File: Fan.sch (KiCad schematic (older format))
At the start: 0 parts

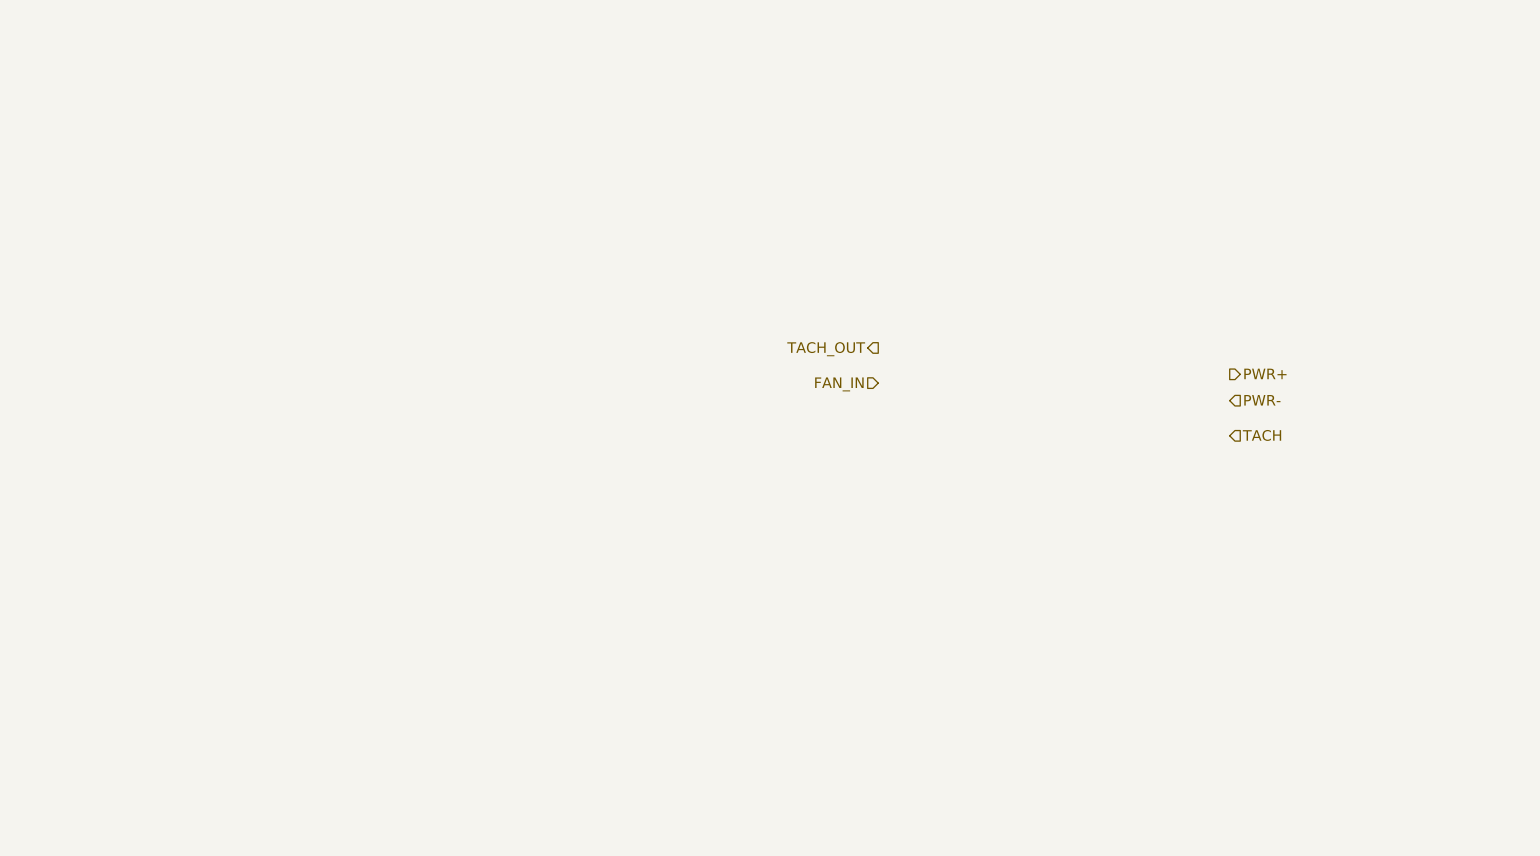
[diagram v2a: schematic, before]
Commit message: Created first schematic for Fan Driver module
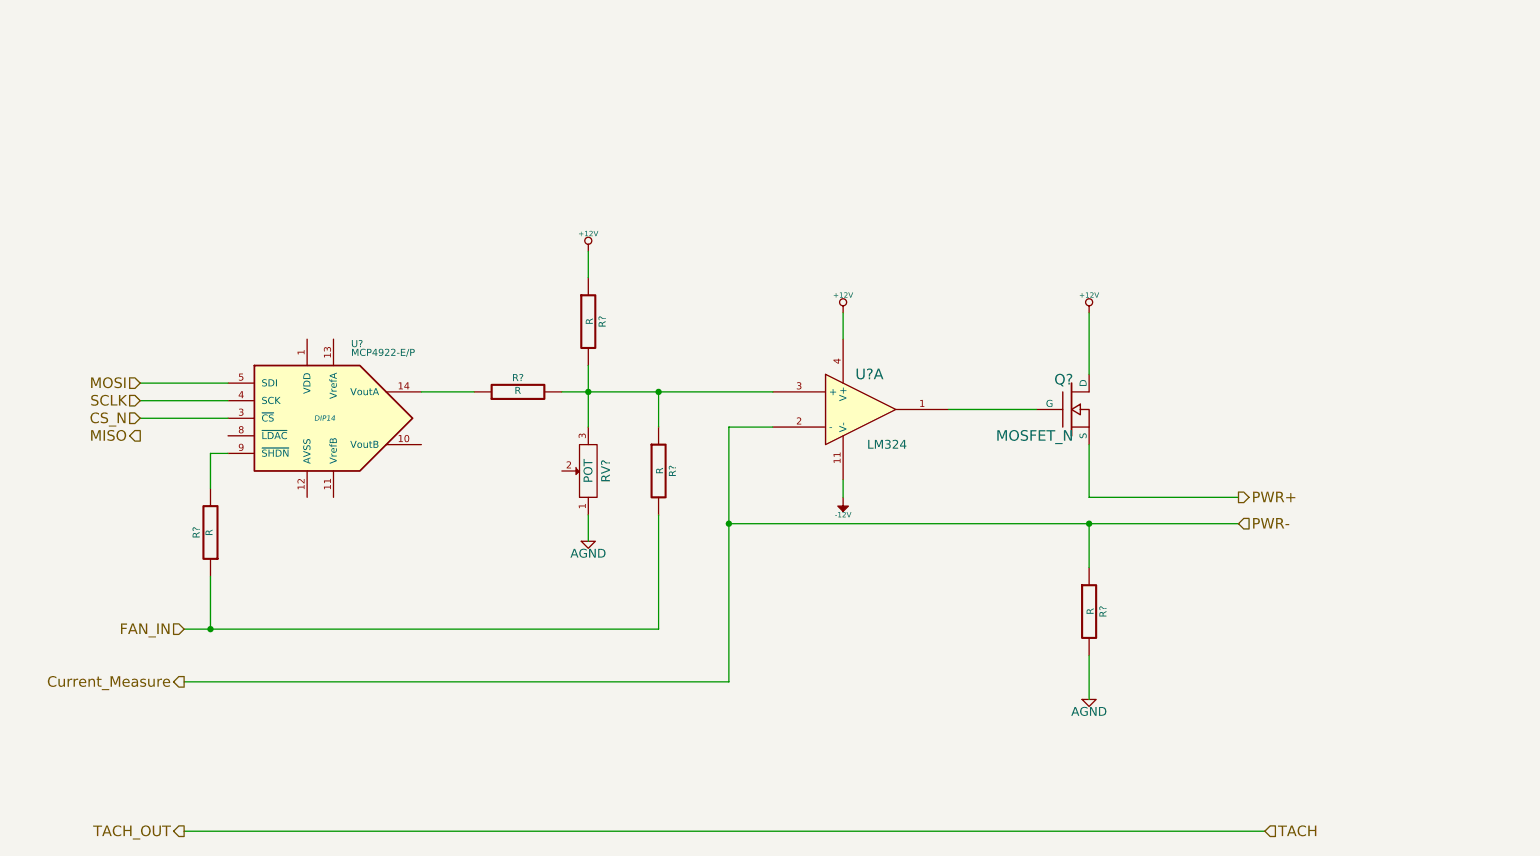
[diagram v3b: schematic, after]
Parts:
- added Q?: MOSFET_N, ~, symbol MOSFET_N
- added R? (x5): R, ~, symbol R
- added RV?: POT, ~, symbol POT
- added U?: LM324, ~, symbol LM324
- added U?: MCP4922-E/P, DIP14, symbol MCP4922-E/P
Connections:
- net FAN_IN: now also R?.1, R?.2
- net PWR+: now also Q?.S
- new net: Q?.G, U?.1
- new net: R?.1, R?.2, R?.2, RV?.3, U?.3 (+)
- new net: R?.1, U?.14 (VoutA)
- new net: R?.2, U?.9 (~SHDN~)
- new net +12V: Q?.D, R?.1, U?.4 (V+)
- new net -12V: U?.11 (V-)
- new net AGND: R?.2, RV?.1
- new net CS_N: U?.3 (~CS~)
- new net Current_Measure: R?.1, U?.2 (-)
- new net MOSI: U?.5 (SDI)
- new net SCLK: U?.4 (SCK)

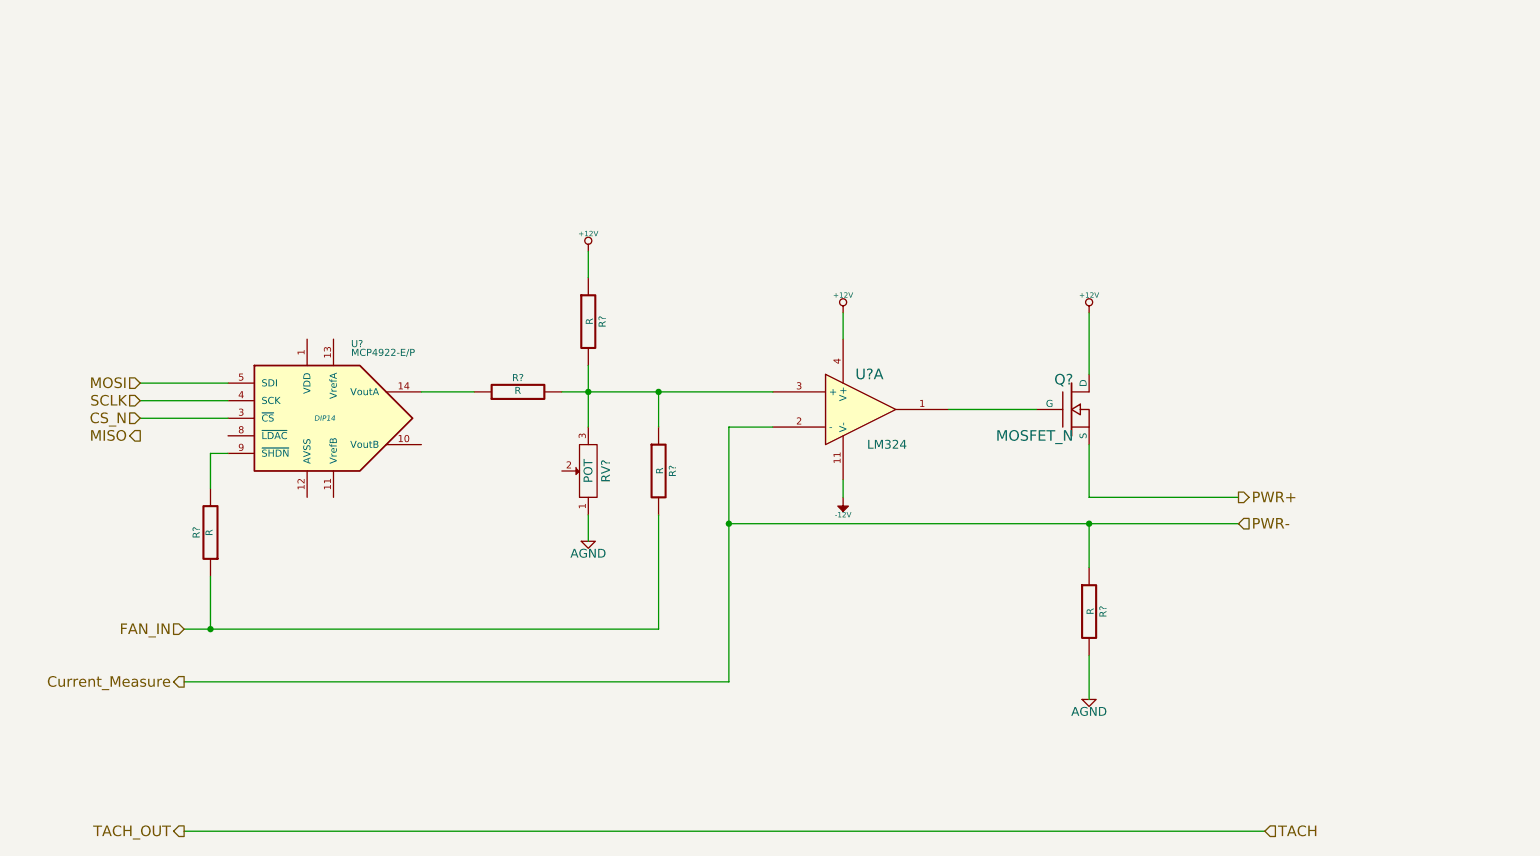
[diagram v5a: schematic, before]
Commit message: Created the Arduino module and then connected all the modules in the main schematic
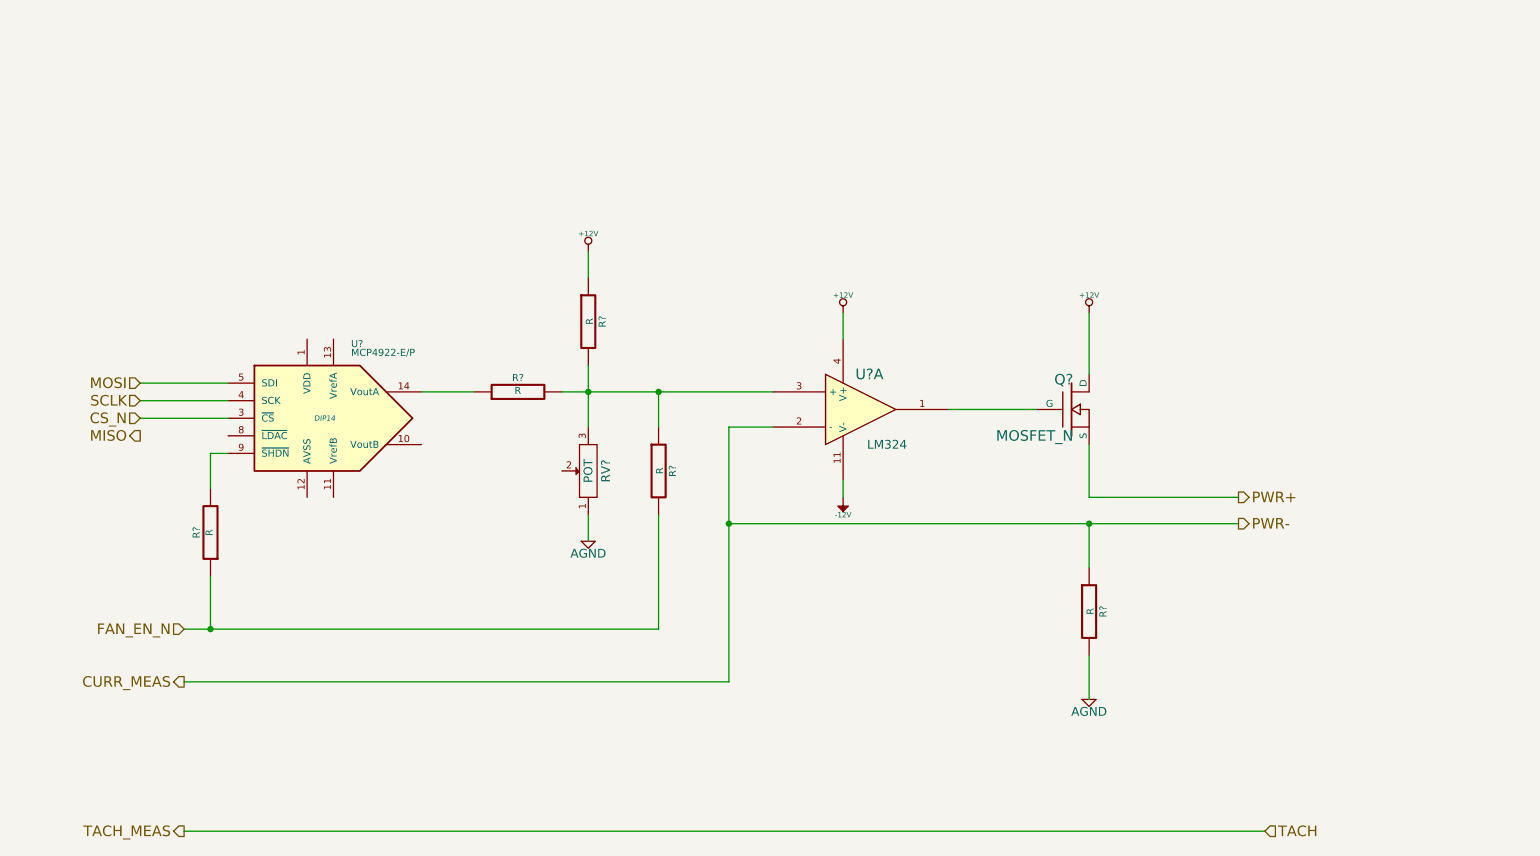
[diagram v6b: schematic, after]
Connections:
- net Current_Measure renamed CURR_MEAS
- net FAN_IN renamed FAN_EN_N
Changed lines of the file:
@@
 $Descr A4 11693 8268
 encoding utf-8
-Sheet 7 9
+Sheet 6 9
 Title ""
 Date "10 feb 2014"
@@
 Text HLabel 8500 3250 2    60   Output ~ 0
 PWR+
-Text HLabel 8500 3400 2    60   Input ~ 0
+Text HLabel 8500 3400 2    60   Output ~ 0
 PWR-
 Text HLabel 2500 5150 0    60   Output ~ 0
-TACH_OUT
+TACH_MEAS
 Text HLabel 2500 4000 0    60   Input ~ 0
-FAN_IN
+FAN_EN_N
 Text HLabel 8650 5150 2    60   Input ~ 0
 TACH
@@
 	2500 5150 8650 5150
 Text HLabel 2500 4300 0    60   Output ~ 0
-Current_Measure
+CURR_MEAS
 Wire Wire Line
 	5600 4300 2500 4300

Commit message: Modified the FAN module and corresponding pins in Arduino module
1) Added FAN_MODE
2) Changed FAN_EN_N to FAN_PWM
3) Used one of the digital PWM pins for FAN_PWM
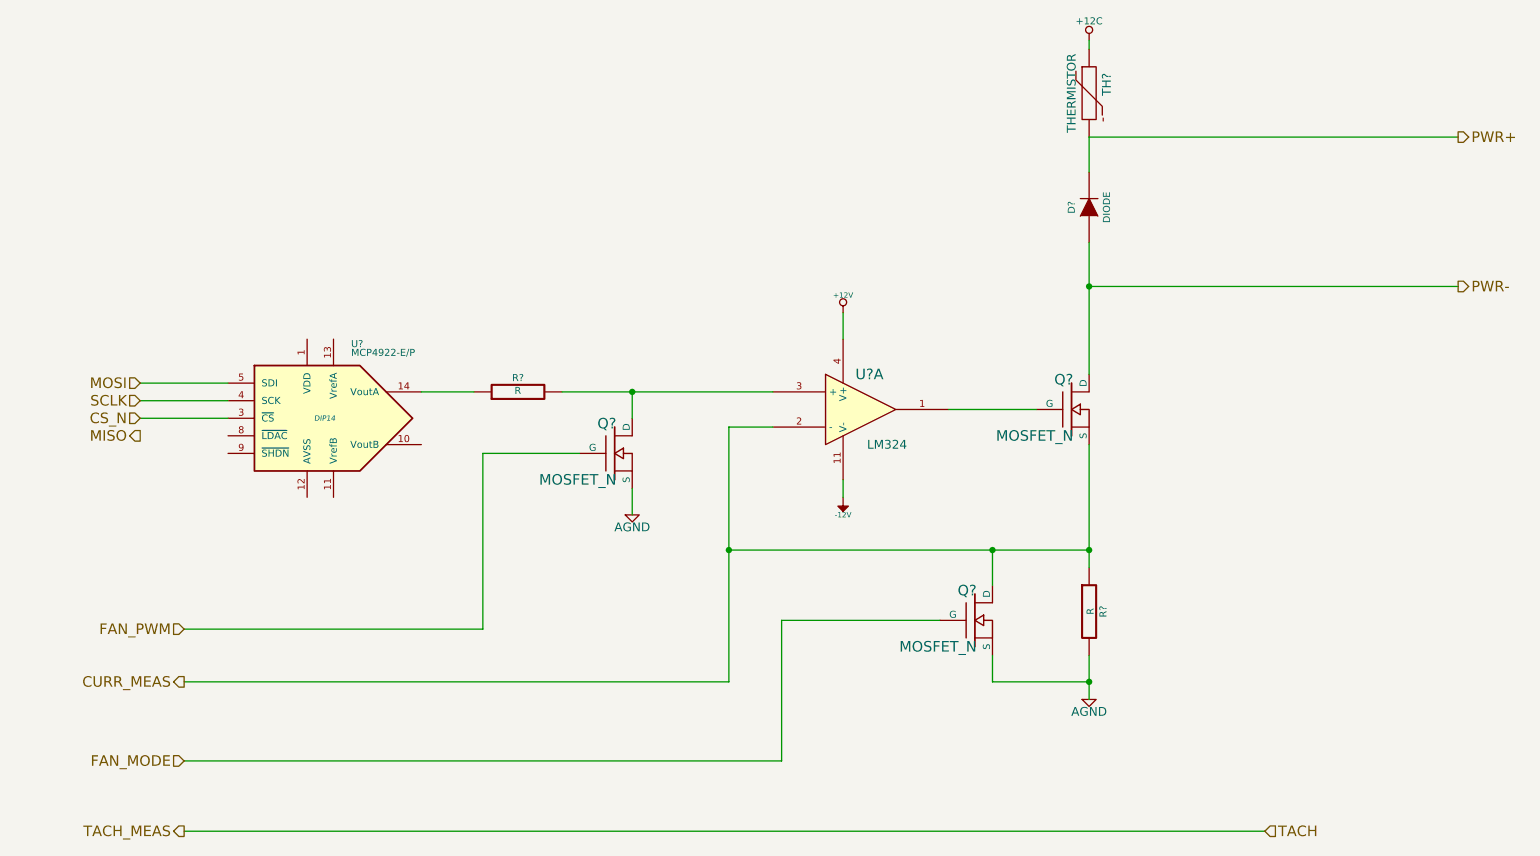
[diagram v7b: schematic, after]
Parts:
- removed R? (x3): R, ~, symbol R
- removed RV?: POT, ~, symbol POT
- added D?: DIODE, ~, symbol DIODE
- added Q? (x2): MOSFET_N, ~, symbol MOSFET_N
- added TH?: THERMISTOR, ~, symbol THERMISTOR
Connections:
- net +12V: no longer Q?.D
- net AGND: now also Q?.S, Q?.S
- net CURR_MEAS: now also Q?.S, Q?.D
- net PWR+: now also D?.2 (K), TH?.2; no longer Q?.S
- net at R?.2, U?.3 (+): now also Q?.D
- new net +12C: TH?.1
- new net FAN_MODE: Q?.G
- new net FAN_PWM: Q?.G
- new net PWR-: D?.1 (A), Q?.D
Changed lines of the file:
@@
 Sheet 6 9
 Title ""
-Date "10 feb 2014"
+Date "11 feb 2014"
 Rev ""
 Comp ""
@@
 Comment4 ""
 $EndDescr
-Text HLabel 8500 3250 2    60   Output ~ 0
+Text HLabel 9750 1200 2    60   Output ~ 0
 PWR+
-Text HLabel 8500 3400 2    60   Output ~ 0
+Text HLabel 9750 2050 2    60   Output ~ 0
 PWR-
 Text HLabel 2500 5150 0    60   Output ~ 0
 TACH_MEAS
 Text HLabel 2500 4000 0    60   Input ~ 0
-FAN_EN_N
+FAN_PWM
 Text HLabel 8650 5150 2    60   Input ~ 0
 TACH
@@
 Wire Wire Line
 	6850 2750 7350 2750
-$Comp
-L +12V #PWR?
-U 1 1 52F5F80E
-P 7650 2200
-F 0 "#PWR?" H 7650 2150 20  0001 C CNN
-F 1 "+12V" H 7650 2300 30  0000 C CNN
-F 2 "" H 7650 2200 60  0000 C CNN
-F 3 "" H 7650 2200 60  0000 C CNN
-	1    7650 2200
-	1    0    0    -1
-$EndComp
-Wire Wire Line
-	7650 2950 7650 3250
-Wire Wire Line
-	7650 3250 8500 3250
+Wire Wire Line
+	7650 2950 7650 3550
+Wire Wire Line
+	7650 3550 7650 3650
 $Comp
 L R R?
@@
 	1    0    0    -1
 $EndComp
-Wire Wire Line
-	5600 3400 8500 3400
-Wire Wire Line
-	7650 3400 7650 3650
 $Comp
 L AGND #PWR?
@@
 $EndComp
 Wire Wire Line
-	7650 4150 7650 4400
+	7650 4150 7650 4300
+Wire Wire Line
+	7650 4300 7650 4400
 Wire Wire Line
 	5850 2850 5600 2850
 Wire Wire Line
-	5600 2850 5600 4300
-Connection ~ 7650 3400
+	5600 2850 5600 3550
+Wire Wire Line
+	5600 3550 5600 4300
 $Comp
 L -12V #PWR?
@@
 Wire Wire Line
 	6250 2200 6250 2350
-Wire Wire Line
-	7650 2200 7650 2550
-Wire Wire Line
-	4650 2650 5850 2650
-$Comp
-L POT RV?
-U 1 1 52F5F895
-P 4800 3100
-F 0 "RV?" H 4800 3000 50  0000 C CNN
-F 1 "POT" H 4800 3100 50  0000 C CNN
-F 2 "~" H 4800 3100 60  0000 C CNN
-F 3 "~" H 4800 3100 60  0000 C CNN
-	1    4800 3100
-	0    -1   -1   0
-$EndComp
-$Comp
-L R R?
-U 1 1 52F5F8A4
-P 4800 2250
-F 0 "R?" V 4880 2250 40  0000 C CNN
-F 1 "R" V 4807 2251 40  0000 C CNN
-F 2 "~" V 4730 2250 30  0000 C CNN
-F 3 "~" H 4800 2250 30  0000 C CNN
-	1    4800 2250
-	1    0    0    -1
-$EndComp
-$Comp
-L +12V #PWR?
-U 1 1 52F5F8B1
-P 4800 1850
-F 0 "#PWR?" H 4800 1800 20  0001 C CNN
-F 1 "+12V" H 4800 1950 30  0000 C CNN
-F 2 "" H 4800 1850 60  0000 C CNN
-F 3 "" H 4800 1850 60  0000 C CNN
-	1    4800 1850
-	1    0    0    -1
-$EndComp
-Wire Wire Line
-	4800 1850 4800 2000
-Wire Wire Line
-	4800 2500 4800 2850
-Connection ~ 4800 2650
 $Comp
 L AGND #PWR?
 U 1 1 52F5F8F6
-P 4800 3500
-F 0 "#PWR?" H 4800 3500 40  0001 C CNN
-F 1 "AGND" H 4800 3430 50  0000 C CNN
-F 2 "" H 4800 3500 60  0000 C CNN
-F 3 "" H 4800 3500 60  0000 C CNN
-	1    4800 3500
-	1    0    0    -1
-$EndComp
-Wire Wire Line
-	4800 3350 4800 3500
+P 5050 3350
+F 0 "#PWR?" H 5050 3350 40  0001 C CNN
+F 1 "AGND" H 5050 3280 50  0000 C CNN
+F 2 "" H 5050 3350 60  0000 C CNN
+F 3 "" H 5050 3350 60  0000 C CNN
+	1    5050 3350
+	1    0    0    -1
+$EndComp
+Wire Wire Line
+	5050 3200 5050 3350
 $Comp
 L MCP4922-E/P U?
@@
 Wire Wire Line
 	5600 4300 2500 4300
-Connection ~ 5600 3400
-$Comp
-L R R?
-U 1 1 52F5F963
-P 5200 3100
-F 0 "R?" V 5280 3100 40  0000 C CNN
-F 1 "R" V 5207 3101 40  0000 C CNN
-F 2 "~" V 5130 3100 30  0000 C CNN
-F 3 "~" H 5200 3100 30  0000 C CNN
-	1    5200 3100
-	1    0    0    -1
-$EndComp
-Wire Wire Line
-	2500 4000 5200 4000
-Wire Wire Line
-	5200 4000 5200 3350
-Wire Wire Line
-	5200 2850 5200 2650
-Connection ~ 5200 2650
 $Comp
 L R R?
@@
 	2250 2800 2750 2800
 $Comp
-L R R?
-U 1 1 52F5FA3A
-P 2650 3450
-F 0 "R?" V 2730 3450 40  0000 C CNN
-F 1 "R" V 2657 3451 40  0000 C CNN
-F 2 "~" V 2580 3450 30  0000 C CNN
-F 3 "~" H 2650 3450 30  0000 C CNN
-	1    2650 3450
-	-1   0    0    1
-$EndComp
-Wire Wire Line
-	2650 3200 2650 3000
-Wire Wire Line
-	2650 3000 2750 3000
-Wire Wire Line
-	2650 3700 2650 4000
-Connection ~ 2650 4000
+L MOSFET_N Q?
+U 1 1 52F9D0E4
+P 7000 3950
+F 0 "Q?" H 7010 4120 60  0000 R CNN
+F 1 "MOSFET_N" H 7010 3800 60  0000 R CNN
+F 2 "~" H 7000 3950 60  0000 C CNN
+F 3 "~" H 7000 3950 60  0000 C CNN
+	1    7000 3950
+	1    0    0    -1
+$EndComp
+$Comp
+L THERMISTOR TH?
+U 1 1 52F9D118
+P 7650 950
+F 0 "TH?" V 7750 1000 50  0000 C CNN
+F 1 "THERMISTOR" V 7550 950 50  0000 C CNN
+F 2 "~" H 7650 950 60  0000 C CNN
+F 3 "~" H 7650 950 60  0000 C CNN
+	1    7650 950
+	1    0    0    -1
+$EndComp
+Wire Wire Line
+	7650 700  7650 650
+Wire Wire Line
+	7650 1200 9750 1200
+Wire Wire Line
+	9750 2050 7650 2050
+Wire Wire Line
+	7650 1800 7650 2050
+Wire Wire Line
+	7650 2050 7650 2550
+$Comp
+L DIODE D?
+U 1 1 52F9D192
+P 7650 1600
+F 0 "D?" H 7650 1700 40  0000 C CNN
+F 1 "DIODE" H 7650 1500 40  0000 C CNN
+F 2 "~" H 7650 1600 60  0000 C CNN
+F 3 "~" H 7650 1600 60  0000 C CNN
+	1    7650 1600
+	0    -1   -1   0
+$EndComp
+Wire Wire Line
+	7650 1400 7650 1200
+Connection ~ 7650 2050
+Connection ~ 7650 3550
+Connection ~ 5600 3550
+Wire Wire Line
+	7100 4300 7650 4300
+Connection ~ 7650 4300
+Wire Wire Line
+	4650 2650 5050 2650
+Wire Wire Line
+	5050 2650 5850 2650
+$Comp
+L MOSFET_N Q?
+U 1 1 52F9D29A
+P 4950 3000
+F 0 "Q?" H 4960 3170 60  0000 R CNN
+F 1 "MOSFET_N" H 4960 2850 60  0000 R CNN
+F 2 "~" H 4950 3000 60  0000 C CNN
+F 3 "~" H 4950 3000 60  0000 C CNN
+	1    4950 3000
+	1    0    0    -1
+$EndComp
+Wire Wire Line
+	5050 2800 5050 2650
+Connection ~ 5050 2650
+Wire Wire Line
+	4750 3000 4200 3000
+Wire Wire Line
+	4200 3000 4200 4000
+Wire Wire Line
+	4200 4000 2500 4000
+Text HLabel 2500 4750 0    60   Input ~ 0
+FAN_MODE
+Wire Wire Line
+	5600 3550 7100 3550
+Wire Wire Line
+	7100 3550 7650 3550
+Wire Wire Line
+	7100 3750 7100 3550
+Connection ~ 7100 3550
+Wire Wire Line
+	7100 4150 7100 4300
+Wire Wire Line
+	6800 3950 5900 3950
+Wire Wire Line
+	5900 3950 5900 4750
+Wire Wire Line
+	5900 4750 2500 4750
+$Comp
+L +12C #PWR?
+U 1 1 52F9D6B5
+P 7650 650
+F 0 "#PWR?" H 7650 620 30  0001 C CNN
+F 1 "+12C" H 7650 760 40  0000 C CNN
+F 2 "" H 7650 650 60  0000 C CNN
+F 3 "" H 7650 650 60  0000 C CNN
+	1    7650 650
+	1    0    0    -1
+$EndComp
 $EndSCHEMATC
